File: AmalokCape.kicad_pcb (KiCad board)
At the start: 4 copper layers, 100 x 85 mm, 13 parts, among them J1 PowerBoost_1000C, J2 FONA800H, J3 UltimateGPS, J4 Conn_01x02_Male, J5 Conn_01x02_Male, SW1 SW_Push

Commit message: [add]	Power management circuit [add]	New PCB footprints distribution
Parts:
- added D3: 1N4001, Diode_THT:D_DO-41_SOD81_P10.16mm_Horizontal, F.Cu at (233.0, 62.0)
- added D4: LED3, LED_THT:LED_D3.0mm, F.Cu at (245.0, 100.0)
- added J6: USB_A, connectors:USB_A_0482580001, F.Cu at (217.2, 101.0)
- added J8: USB_B_Mini, connectors:USB_Mini_B_Female_XM7D-0512, F.Cu at (229.2, 30.7)
- added Q1: 2N3904, Package_TO_SOT_THT:TO-92_Inline, F.Cu at (240.0, 74.0)
- added R3: 1kOhm, Resistor_THT:R_Axial_DIN0207_L6.3mm_D2.5mm_P7.62mm_Horizontal, F.Cu at (192.4, 58.0)
- added R5: 330Ohm, Resistor_THT:R_Axial_DIN0207_L6.3mm_D2.5mm_P7.62mm_Horizontal, F.Cu at (245.0, 87.4)
- added R6: 1kOhm, Resistor_THT:R_Axial_DIN0207_L6.3mm_D2.5mm_P7.62mm_Horizontal, F.Cu at (237.0, 69.6)
- added R7: 3kOhm, Resistor_THT:R_Axial_DIN0207_L6.3mm_D2.5mm_P7.62mm_Horizontal, F.Cu at (248.6, 80.0)
- added R8: 5kOhm, Resistor_THT:R_Axial_DIN0207_L6.3mm_D2.5mm_P7.62mm_Horizontal, F.Cu at (241.0, 83.5)
- added RLY1: EC2-5NU, digikey-footprints:Relay_THT_EC2, F.Cu at (229.0, 67.1)
- added SW2: SW_Push, Button_Switch_THT:SW_Tactile_SPST_Angled_PTS645Vx83-2LFS, F.Cu at (247.0, 108.0)
- added U1: ATtiny85-20PU, Package_DIP:DIP-8_W7.62mm, F.Cu at (241.5, 70.0)
- D1: value LED -> LED1
- D2: value LED -> LED2
- SW1: footprint Button_Switch_THT:SW_PUSH_6mm -> Button_Switch_THT:SW_Tactile_SPST_Angled_PTS645Vx83-2LFS
- moved D2 225.2 mm to (240.0, 100.0), turned to 90 degrees
- moved D1 218.8 mm to (235.0, 100.0), turned to 90 degrees
- moved SW1 211.7 mm to (236.0, 108.0), turned to 180 degrees
- moved J1 207.5 mm to (227.2, 53.2)
- moved R4 206.7 mm to (240.0, 87.4), turned to 270 degrees
- moved J4 205.7 mm to (237.4, 57.4), turned to 270 degrees
- moved R1 200.4 mm to (235.0, 87.4), turned to 270 degrees
- moved R2 163.8 mm to (188.4, 92.8)
- moved P1 129.6 mm to (178.6, 99.4), turned to 0 degrees
- moved J5 123.4 mm to (216.5, 72.2), turned to 90 degrees
- moved J3 118.1 mm to (189.2, 64.5), turned to 90 degrees
- moved P2 108.9 mm to (178.6, 74.0), turned to 0 degrees
- moved J2 46.4 mm to (155.6, 65.0), turned to 90 degrees
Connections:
- J1 pad 1: Net-(J1-Pad1) -> /Vusb
- J1 pad 5: Net-(J1-Pad5) -> GND
- J1 pad 6: Net-(J1-Pad6) -> /LBO
- J1 pad 8: VDD_5V -> /5Vin
- P1 pad 13: /(U1.L14)USB1.ID -> GND
- R1 pad 1: /(U1.R5)GPIO-0.26 -> /(U1.F1)
- R2 pad 2: /(U1.B10)I2C2.SDA -> /(U1.A2)PRU-0.1
- SW1 pad 1: /(U1.B10)I2C2.SDA -> /(U1.A2)PRU-0.1
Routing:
- net GND: track 267.7 -> 0.00 mm
- net VDD_5V: track 132.4 -> 0.00 mm
- net /Vbat: track 98.2 -> 0.00 mm
- net VDD_3V3B: track 86.2 -> 0.00 mm, vias 2 -> 0
- net /(U1.B10)I2C2.SDA: track 49.0 -> 0.00 mm
- net /(U1.B11)I2C1.SCL: track 42.9 -> 0.00 mm
- net /(U1.A11)I2C1.SDA: track 37.5 -> 0.00 mm
- net /EN: track 34.6 -> 0.00 mm
- net /(U1.R16)UART4.TX: track 19.6 -> 0.00 mm
- net /(U1.P15)UART4.RX: track 19.6 -> 0.00 mm
- net /(U1.T16): track 17.5 -> 0.00 mm
- net /(U1.T15): track 17.5 -> 0.00 mm
- net /(U1.R15): track 17.5 -> 0.00 mm
- net /(U1.P7)PRU-0.15: track 17.4 -> 0.00 mm
- net /(U1.R5)GPIO-0.26: track 12.0 -> 0.00 mm
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- removed copper zone on B.Cu, net GND
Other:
- board size 100 x 85 mm -> 120 x 90 mm
- board text added: "v0.4"
- board text removed: "v0.3"

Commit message: [add]	V0.4 layout
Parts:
- moved D1 118.6 mm to (116.4, 103.2)
- moved D2 118.6 mm to (121.4, 103.2)
- moved D3 118.6 mm to (114.4, 65.2)
- moved D4 118.6 mm to (126.4, 103.2)
- moved J1 118.6 mm to (108.7, 56.4)
- moved J2 118.6 mm to (37.0, 68.2)
- moved J4 118.6 mm to (118.8, 60.6)
- moved J5 118.6 mm to (97.9, 75.4)
- moved J6 118.6 mm to (98.6, 104.2)
- moved J8 118.6 mm to (110.6, 33.8)
- moved P1 118.6 mm to (60.0, 102.5)
- moved P2 118.6 mm to (60.0, 77.1)
- moved Q1 118.6 mm to (121.4, 77.2)
- moved R1 118.6 mm to (116.4, 90.6)
- moved R3 118.6 mm to (73.8, 61.2)
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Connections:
- R1 pad 1: /(U1.F1) -> /(U1.R5)GPIO-0.26
- R2 pad 2: /(U1.A2)PRU-0.1 -> /(U1.F1)
- R5 pad 1: /(U1.R5)GPIO-0.26 -> /(U1.A2)PRU-0.1
- SW1 pad 1: /(U1.A2)PRU-0.1 -> /(U1.F1)
- U1 pad 5: /Relay -> /Vusb
- U1 pad 7: /Vusb -> /Relay
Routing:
- net GND: track 0.00 -> 524.5 mm
- net VDD_3V3B: track 0.00 -> 110.8 mm, vias 0 -> 4
- net /(U1.B13)SPI0.MISO: track 0.00 -> 97.1 mm
- net /(U1.A13)SPI0.CLK: track 0.00 -> 87.8 mm
- net /VinPB: track 0.12 -> 83.0 mm
- net /Vbat: track 0.00 -> 82.0 mm
- net /Vusb: track 0.00 -> 57.7 mm, vias 0 -> 2
- net /(U1.B11)I2C1.SCL: track 0.00 -> 55.0 mm
- net USB_DC: track 0.00 -> 54.7 mm
- net /Reset: track 0.00 -> 53.3 mm
- net /(U1.A2)PRU-0.1: track 0.00 -> 52.8 mm
- net /(U1.L16)USB1.D-: track 0.00 -> 52.5 mm
- net /(U1.L15)USB1.D+: track 0.00 -> 52.1 mm
- net /5Vin: track 0.00 -> 52.1 mm
- net /(U1.F1): track 0.00 -> 46.6 mm
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- added copper zone on B.Cu, net GND
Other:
- net class Default: clearance 0.2 -> 0.16
- rule trace_clearance: 0.2 -> 0.16

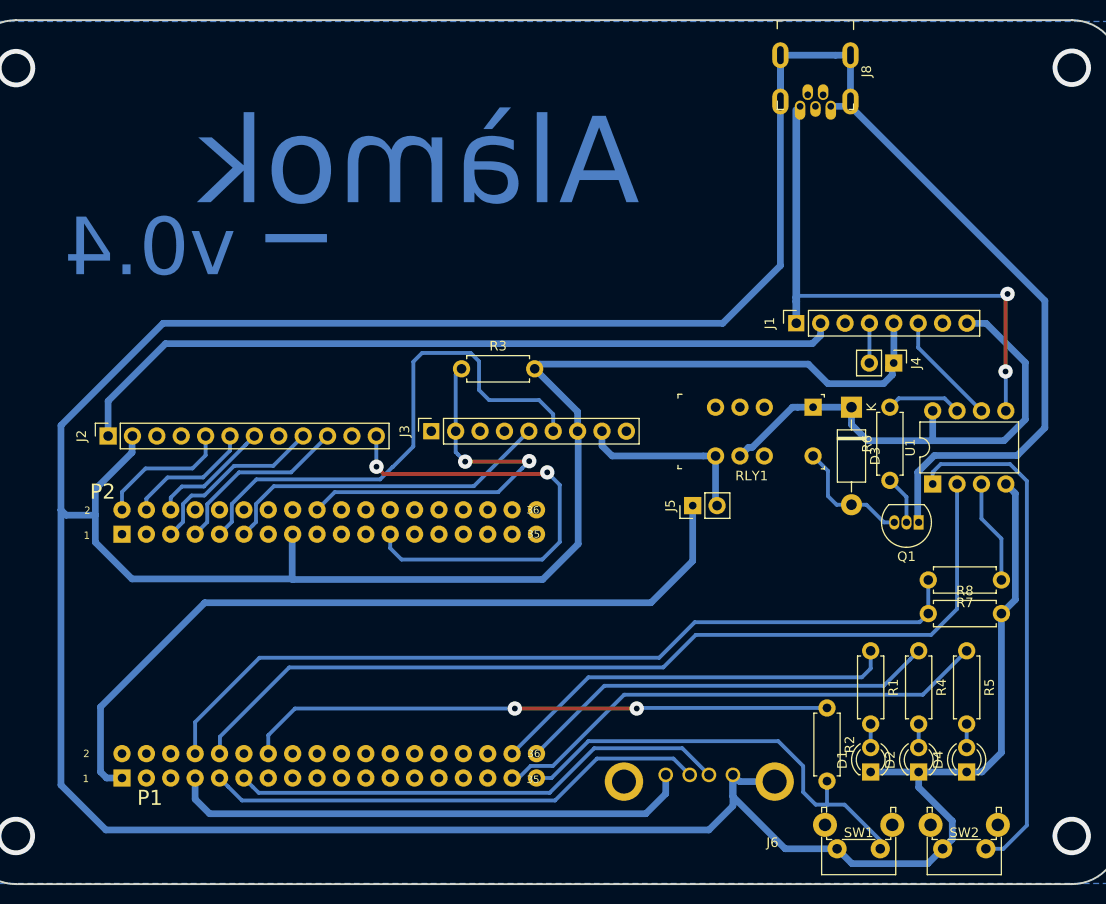
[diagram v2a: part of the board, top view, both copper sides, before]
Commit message: [fix]	USB connector pins 	Vias size
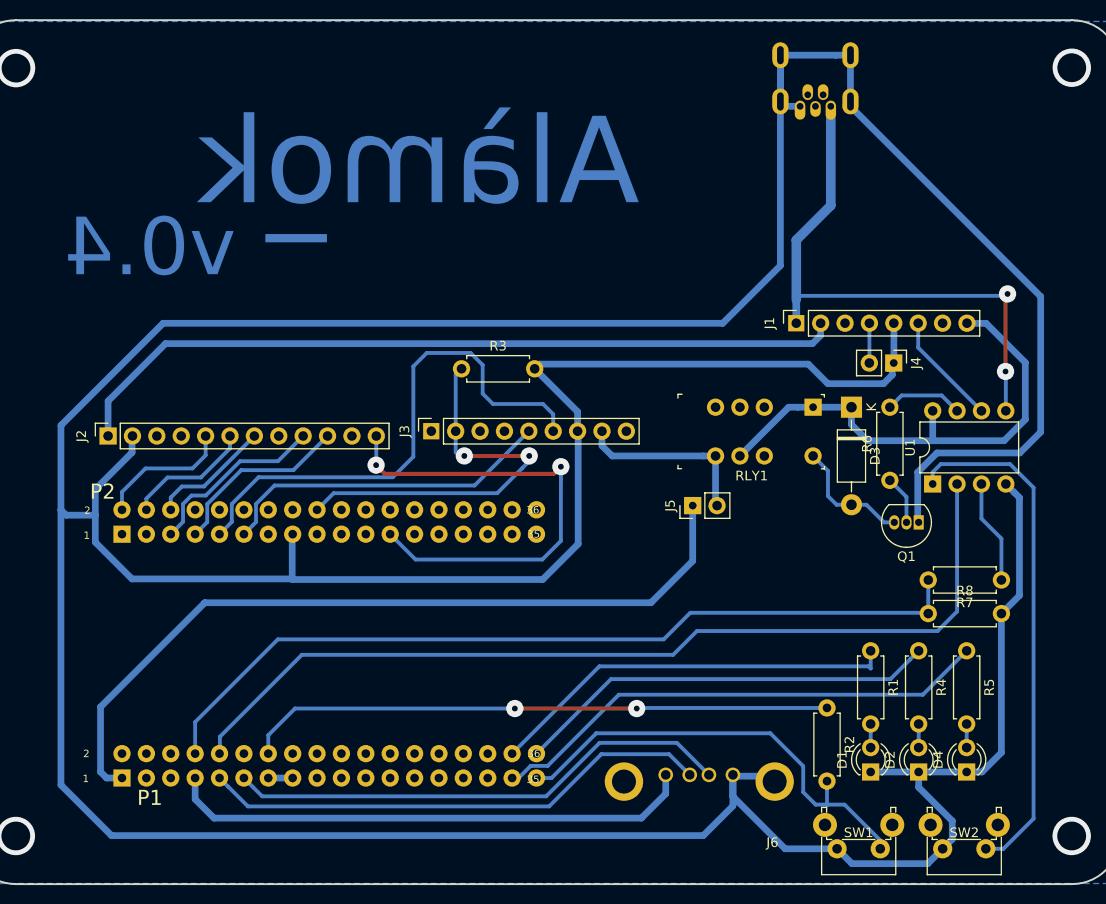
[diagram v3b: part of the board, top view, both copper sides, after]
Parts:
- J8: moved to B.Cu
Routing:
- net GND: track 524.5 -> 528.8 mm
- net /Vusb: track 57.7 -> 59.3 mm
- net /(U1.L16)USB1.D-: track 52.5 -> 53.4 mm
- net VDD_3V3B: track 110.8 -> 111.6 mm
- net /(U1.L15)USB1.D+: track 52.1 -> 52.9 mm
- net /(U1.F1): track 46.6 -> 47.3 mm
- net /Reset: track 53.3 -> 53.9 mm
